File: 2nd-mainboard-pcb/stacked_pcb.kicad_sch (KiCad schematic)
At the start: 7 parts, among them J17 Steckverbinder_Male_1, J18 Steckverbinder_Male_2, J19 Steckverbinder_Female_2

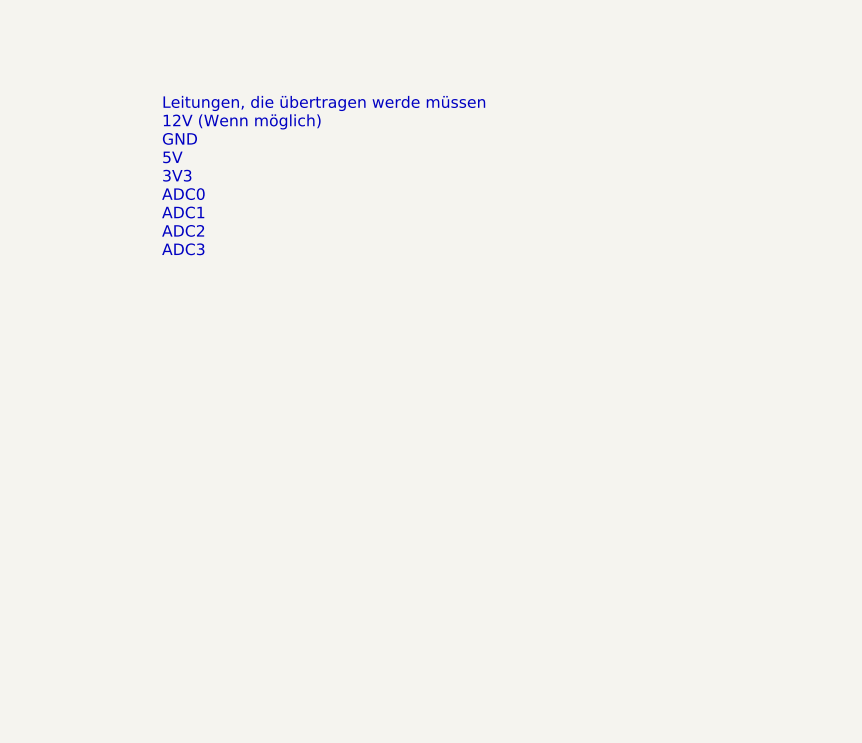
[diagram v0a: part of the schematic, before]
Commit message: added imported components, changed structure
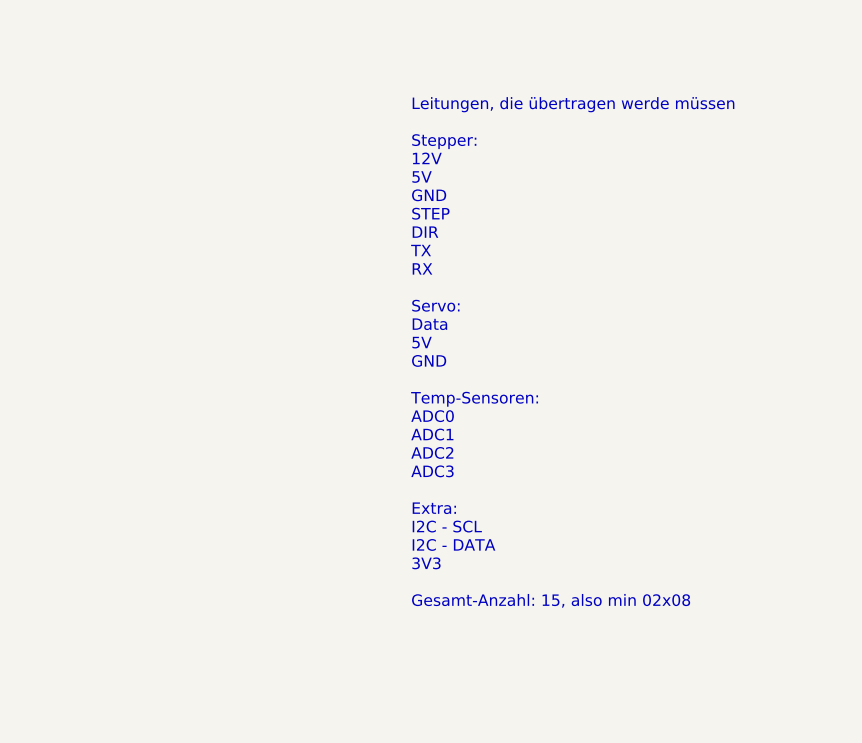
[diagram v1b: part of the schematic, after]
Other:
- note added: "Leitungen, die übertragen werde müssen Stepper: 12V 5V GND STEP DIR TX RX Servo: Data 5V GND Temp-Sensoren: ADC0 ADC1 ADC2 ADC3 Extra: I2C - SCL I2C - DATA 3V3 Gesamt-Anzahl: 15, also min 02x08"
- note removed: "Leitungen, die übertragen werde müssen 12V (Wenn möglich) GND 5V 3V3 ADC0 ADC1 ADC2 ADC3"
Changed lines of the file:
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@@
 		)
 	)
-	(text "Leitungen, die übertragen werde müssen\n12V (Wenn möglich)\nGND\n5V\n3V3\nADC0\nADC1\nADC2\nADC3\n"
+	(text "Leitungen, die übertragen werde müssen\n\nStepper:\n12V\n5V\nGND\nSTEP\nDIR\nTX\nRX\n\nServo:\nData\n5V\nGND\n\nTemp-Sensoren:\nADC0\nADC1\nADC2\nADC3\n\nExtra:\nI2C - SCL\nI2C - DATA\n3V3\n\nGesamt-Anzahl: 15, also min 02x08\n"
 		(exclude_from_sim no)
-		(at 205.74 35.814 0)
+		(at 233.426 55.372 0)
 		(effects
 			(font

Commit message: finished stacked design, annotaded
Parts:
- removed J18: Steckverbinder_Male_2, CustomFotLibByJan:BF100-16-A-D-1-0640-L-C, symbol Connector_Generic:Conn_02x08_Row_Letter_First
- added J21: Steckverbinder_Male_2, CustomFotLibByJan:BF100-16-A-D-1-0640-L-C, symbol Connector_Generic:Conn_02x08_Row_Letter_First
- renumbered J17 to J20, J19 to J22
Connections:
- net +12V: now also J22.b2 (Pin_b2), J21.b2 (Pin_b2); no longer J20.a2 (Pin_a2), J22.a7 (Pin_a7), J22.b7 (Pin_b7)
- net +3V3: now also J22.b4 (Pin_b4), J21.b4 (Pin_b4); no longer J20.a4 (Pin_a4), J22.a5 (Pin_a5), J22.b5 (Pin_b5)
- net GND: now also J21.b1 (Pin_b1); no longer J20.a1 (Pin_a1), J20.a8 (Pin_a8), J20.b8 (Pin_b8), J22.a1 (Pin_a1), J22.a8 (Pin_a8), J22.b8 (Pin_b8)
- net SCL: now also J20.a7 (Pin_a7), J22.a7 (Pin_a7), J21.a7 (Pin_a7); no longer J20.a5 (Pin_a5), J20.b5 (Pin_b5), J22.a4 (Pin_a4), J22.b4 (Pin_b4)
- net SDA: now also J20.a8 (Pin_a8), J22.a8 (Pin_a8), J21.a8 (Pin_a8); no longer J20.a6 (Pin_a6), J20.b6 (Pin_b6), J22.a3 (Pin_a3), J22.b3 (Pin_b3)
- removed net +5V: J20.a3 (Pin_a3), J20.b3 (Pin_b3), J22.a6 (Pin_a6), J22.b6 (Pin_b6)
- removed net IO3: J20.a7 (Pin_a7), J20.b7 (Pin_b7), J22.a2 (Pin_a2), J22.b2 (Pin_b2)
- new net +5V_POW: J20.b3 (Pin_b3), J21.b3 (Pin_b3), J22.b3 (Pin_b3)
- new net ADC0: J20.b5 (Pin_b5), J21.b5 (Pin_b5), J22.b5 (Pin_b5)
- new net ADC1: J20.b6 (Pin_b6), J21.b6 (Pin_b6), J22.b6 (Pin_b6)
- new net ADC2: J20.b7 (Pin_b7), J21.b7 (Pin_b7), J22.b7 (Pin_b7)
- new net ADC3: J20.b8 (Pin_b8), J21.b8 (Pin_b8), J22.b8 (Pin_b8)
- new net DIR: J20.a4 (Pin_a4), J21.a4 (Pin_a4), J22.a4 (Pin_a4)
- new net RESET: J20.a3 (Pin_a3), J21.a3 (Pin_a3), J22.a3 (Pin_a3)
- new net RXD: J20.a6 (Pin_a6), J21.a6 (Pin_a6), J22.a6 (Pin_a6)
- new net SM_Servo: J20.a1 (Pin_a1), J21.a1 (Pin_a1), J22.a1 (Pin_a1)
- new net STEP: J20.a2 (Pin_a2), J21.a2 (Pin_a2), J22.a2 (Pin_a2)
- new net TXD: J20.a5 (Pin_a5), J21.a5 (Pin_a5), J22.a5 (Pin_a5)
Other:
- note added: "Leitungen, die übertragen werde müssen Stepper: 12V 5V GND STEP DIR TX RX RESET Servo: Data 5V GND Temp-Sensoren: ADC0 ADC1 ADC2 ADC3 Extra: I2C - SCL I2C - DATA 3V3 Gesamt-Anzahl: 16, also min 02x08 Optional: BL-Touch Servo Data_BLT 5V GND BL-Touch IO BLT_Switch GND"
- note removed: "Leitungen, die übertragen werde müssen Stepper: 12V 5V GND STEP DIR TX RX Servo: Data 5V GND Temp-Sensoren: ADC0 ADC1 ADC2 ADC3 Extra: I2C - SCL I2C - DATA 3V3 Gesamt-Anzahl: 15, also min 02x08"
- moved on the sheet: J20, J22

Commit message: alle bauteile hinzugefügt
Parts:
- added H1, H10, H11, H12, H2, H3, H4, H9: MountHole, MountingHole:MountingHole_2.2mm_M2_Pad_TopBottom, symbol Mechanical:MountingHole_Pad
- added J19: Steckverbinder_Male_2, CustomFotLibByJan:BF100-16-A-D-1-0640-L-C, symbol Connector_Generic:Conn_02x08_Row_Letter_First
- added J20: Steckverbinder_Female_2, CustomFotLibByJan:BF030-16A-B1-0360-0277-0600-LB, symbol Connector_Generic:Conn_02x08_Row_Letter_First
- renumbered H1 to H5, H2 to H6, H3 to H7, H4 to H8, J20 to J16, J21 to J17, J22 to J18
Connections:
- net +12V: now also J19.b2 (Pin_b2), J20.b2 (Pin_b2)
- net +3V3: now also J19.b4 (Pin_b4), J20.b4 (Pin_b4)
- net +5V_POW: now also J19.b3 (Pin_b3), J20.b3 (Pin_b3)
- net ADC0: now also J19.b5 (Pin_b5), J20.b5 (Pin_b5)
- net ADC1: now also J19.b6 (Pin_b6), J20.b6 (Pin_b6)
- net ADC2: now also J19.b7 (Pin_b7), J20.b7 (Pin_b7)
- net ADC3: now also J19.b8 (Pin_b8), J20.b8 (Pin_b8)
- net DIR: now also J19.a4 (Pin_a4), J20.a4 (Pin_a4)
- net GND: now also H1.1, H10.1, H11.1, H12.1, H2.1, H3.1, H4.1, H9.1, J19.b1 (Pin_b1), J20.b1 (Pin_b1)
- net RESET: now also J19.a3 (Pin_a3), J20.a3 (Pin_a3)
- net RXD: now also J19.a6 (Pin_a6), J20.a6 (Pin_a6)
- net SCL: now also J19.a7 (Pin_a7), J20.a7 (Pin_a7)
- net SDA: now also J19.a8 (Pin_a8), J20.a8 (Pin_a8)
- net SM_Servo: now also J19.a1 (Pin_a1), J20.a1 (Pin_a1)
- net STEP: now also J19.a2 (Pin_a2), J20.a2 (Pin_a2)
- net TXD: now also J19.a5 (Pin_a5), J20.a5 (Pin_a5)
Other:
- note added: "Leitungen, die übertragen werde müssen Fans: 12V 5V GND PWM0 PWM1 PWM2 PWM3 Extra: I2C - SCL I2C - DATA 3V3 Gesamt-Anzahl: 16, also min 02x08"
- note added: "Modul 1: Fans"
- note added: "Modul 2: Atmega + Leistungs-Eingänge"
- note added: "Modul 3: Motoren"
- note removed: "Modul 1"
- note removed: "Modul 2"

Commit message: module 1 positioniert
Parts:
- J16: value Steckverbinder_Male_1 -> Steckverbinder_Male_Fans
- J17: value Steckverbinder_Male_2 -> Steckverbinder_Male_Leistung
- J18: value Steckverbinder_Female_2 -> Steckverbinder_Female_Leistung
- J19: value Steckverbinder_Male_2 -> Steckverbinder_Male_Motoren
- J20: value Steckverbinder_Female_2 -> Steckverbinder_Female_Motoren
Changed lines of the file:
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@@
 			)
 		)
-		(property "Value" "Steckverbinder_Male_2"
+		(property "Value" "Steckverbinder_Male_Leistung"
 			(at 120.65 26.67 0)
 			(effects
@@
 			)
 		)
-		(property "Value" "Steckverbinder_Male_1"
+		(property "Value" "Steckverbinder_Male_Fans"
 			(at 46.99 26.67 0)
 			(effects
@@
 			)
 		)
-		(property "Value" "Steckverbinder_Female_2"
+		(property "Value" "Steckverbinder_Female_Motoren"
 			(at 95.25 114.3 0)
 			(effects
@@
 			)
 		)
-		(property "Value" "Steckverbinder_Male_2"
+		(property "Value" "Steckverbinder_Male_Motoren"
 			(at 45.72 114.3 0)
 			(effects
@@
 			)
 		)
-		(property "Value" "Steckverbinder_Female_2"
+		(property "Value" "Steckverbinder_Female_Leistung"
 			(at 170.18 26.67 0)
 			(effects

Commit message: new arrangement pcb
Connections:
- net +12V: now also J18.a2 (Pin_a2); no longer J18.b2 (Pin_b2)
- net +3V3: now also J18.a4 (Pin_a4); no longer J18.b4 (Pin_b4)
- net +5V_POW: now also J18.a3 (Pin_a3); no longer J18.b3 (Pin_b3)
- net ADC0: now also J16.a2 (Pin_a2), J18.b2 (Pin_b2); no longer J16.b5 (Pin_b5), J17.b5 (Pin_b5), J18.b5 (Pin_b5)
- net ADC1: now also J16.a3 (Pin_a3), J18.b3 (Pin_b3); no longer J16.b6 (Pin_b6), J17.b6 (Pin_b6), J18.b6 (Pin_b6)
- net ADC2: now also J16.a6 (Pin_a6), J18.b6 (Pin_b6); no longer J16.b7 (Pin_b7), J17.b7 (Pin_b7), J18.b7 (Pin_b7)
- net ADC3: now also J16.a7 (Pin_a7), J18.b7 (Pin_b7); no longer J16.b8 (Pin_b8), J17.b8 (Pin_b8), J18.b8 (Pin_b8)
- net DIR: no longer J16.a4 (Pin_a4), J18.a4 (Pin_a4)
- net GND: now also J18.a1 (Pin_a1); no longer J18.b1 (Pin_b1)
- net RESET: now also J16.b5 (Pin_b5), J18.a5 (Pin_a5); no longer J16.a3 (Pin_a3), J18.a3 (Pin_a3)
- net RXD: no longer J16.a6 (Pin_a6), J18.a6 (Pin_a6)
- net SCL: now also J16.b8 (Pin_b8), J18.a8 (Pin_a8); no longer J16.a7 (Pin_a7), J18.a7 (Pin_a7)
- net SDA: now also J16.b7 (Pin_b7), J18.a7 (Pin_a7); no longer J16.a8 (Pin_a8), J18.a8 (Pin_a8)
- net SM_Servo: no longer J16.a1 (Pin_a1), J18.a1 (Pin_a1)
- net STEP: no longer J16.a2 (Pin_a2), J18.a2 (Pin_a2)
- net TXD: no longer J16.a5 (Pin_a5), J18.a5 (Pin_a5)
- new net BLT_Servo: J17.b5 (Pin_b5)
- new net BLT_Switch: J17.b6 (Pin_b6)
- new net FAN_01_PWM_clockwise: J16.a5 (Pin_a5), J18.b5 (Pin_b5)
- new net FAN_01_PWM_counterclockwise: J16.a4 (Pin_a4), J18.b4 (Pin_b4)
- new net FAN_2_PWM: J16.a1 (Pin_a1), J18.b1 (Pin_b1)
- new net FAN_3_PWM: J16.a8 (Pin_a8), J18.b8 (Pin_b8)
- new net LED_2: J16.b6 (Pin_b6), J18.a6 (Pin_a6)
- new net LED_3: J17.b7 (Pin_b7)
- new net SMD_TEMP_1: J17.b8 (Pin_b8)
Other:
- moved on the sheet: J16, J17, J18

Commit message: fertgie V1 der Leistungs-Platine
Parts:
- added J24: Steckverbinder_Male_Fans, Imported_Component_Footprints:SAMTEC_TSM-107-04-L-DV, symbol Imported_Component_Symbols:TSM-107-04-L-DV
- added J25: HLE-107-02-L-DV, Imported_Component_Footprints:SAMTEC_HLE-107-02-L-DV, symbol Imported_Component_Symbols:HLE-107-02-L-DV
- added J26: Steckverbinder_Male_Leistung, Imported_Component_Footprints:SAMTEC_TSM-107-04-L-DV, symbol Imported_Component_Symbols:TSM-107-04-L-DV
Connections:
- net ADC0: now also J18.b7 (Pin_b7); no longer J18.b2 (Pin_b2)
- net ADC1: now also J18.b6 (Pin_b6); no longer J18.b3 (Pin_b3)
- net ADC2: now also J18.b3 (Pin_b3); no longer J18.b6 (Pin_b6)
- net ADC3: now also J18.b2 (Pin_b2); no longer J18.b7 (Pin_b7)
- net BLT_Servo: now also J17.a3 (Pin_a3); no longer J17.b5 (Pin_b5)
- net LED_3: now also J17.a8 (Pin_a8); no longer J17.b7 (Pin_b7)
- net RESET: now also J17.b5 (Pin_b5); no longer J17.a3 (Pin_a3)
- net SCL: now also J17.b8 (Pin_b8); no longer J17.a7 (Pin_a7)
- net SDA: now also J17.b7 (Pin_b7); no longer J17.a8 (Pin_a8)
- net SMD_TEMP_1: now also J17.a7 (Pin_a7); no longer J17.b8 (Pin_b8)

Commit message: Fan-PCB-Beginning
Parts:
- removed J16: Steckverbinder_Male_Fans, CustomFotLibByJan:BF100-16-A-D-1-0640-L-C, symbol Connector_Generic:Conn_02x08_Row_Letter_First
- removed J17: Steckverbinder_Male_Leistung, CustomFotLibByJan:BF100-16-A-D-1-0640-L-C, symbol Connector_Generic:Conn_02x08_Row_Letter_First
- removed J18: Steckverbinder_Female_Leistung, CustomFotLibByJan:BF030-16A-B1-0360-0277-0600-LB, symbol Connector_Generic:Conn_02x08_Row_Letter_First
- removed J19: Steckverbinder_Male_Motoren, CustomFotLibByJan:BF100-16-A-D-1-0640-L-C, symbol Connector_Generic:Conn_02x08_Row_Letter_First
- removed J20: Steckverbinder_Female_Motoren, CustomFotLibByJan:BF030-16A-B1-0360-0277-0600-LB, symbol Connector_Generic:Conn_02x08_Row_Letter_First
- added J15: Steckverbinder_Female_Motoren, Imported_Component_Footprints:SAMTEC_HLE-107-02-L-DV, symbol Imported_Component_Symbols:HLE-107-02-L-DV
- J13: renamed from J25; value HLE-107-02-L-DV -> Steckverbinder_Female_Leistung
- renumbered J24 to J12, J26 to J14
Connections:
- net +12V: now also J12.03, J13.03, J14.03, J15.03
- net +5V_POW: now also J12.05, J13.05, J14.05, J15.05
- net ADC0: now also J12.08, J13.06, J15.08
- net ADC1: now also J12.10, J13.08, J15.10
- net ADC2: now also J12.12, J13.10, J15.12
- net ADC3: now also J12.14, J13.12, J15.14
- net BLT_Servo: now also J14.10
- net BLT_Switch: now also J14.12
- net DIR: now also J14.08
- net FAN_01_PWM_clockwise: now also J12.04, J13.07, J15.04
- net FAN_01_PWM_counterclockwise: now also J12.02, J13.09, J15.02
- net FAN_2_PWM: now also J12.13, J13.13, J15.06
- net FAN_3_PWM: now also J12.11, J13.11, J15.11
- net GND: now also J12.01, J13.01, J14.01, J15.01
- net LED_2: now also J12.09, J13.04
- net LED_3: now also J14.11, J15.07
- net RESET: now also J15.09
- net RXD: now also J14.04
- net SCL: now also J14.14
- net SDA: now also J14.02
- net SM_Servo: now also J14.09
- net STEP: now also J14.07
- net TXD: now also J14.06
- net SMD_TEMP_0: now reaches J12.06
- net SMD_TEMP_0: now also J13.14, J15.13
- net +5V_USBC: now reaches J12.07
- net +5V_USBC: now also J13.02
- no-connect marks 0 -> 1
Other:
- moved on the sheet: J12, J13, J14

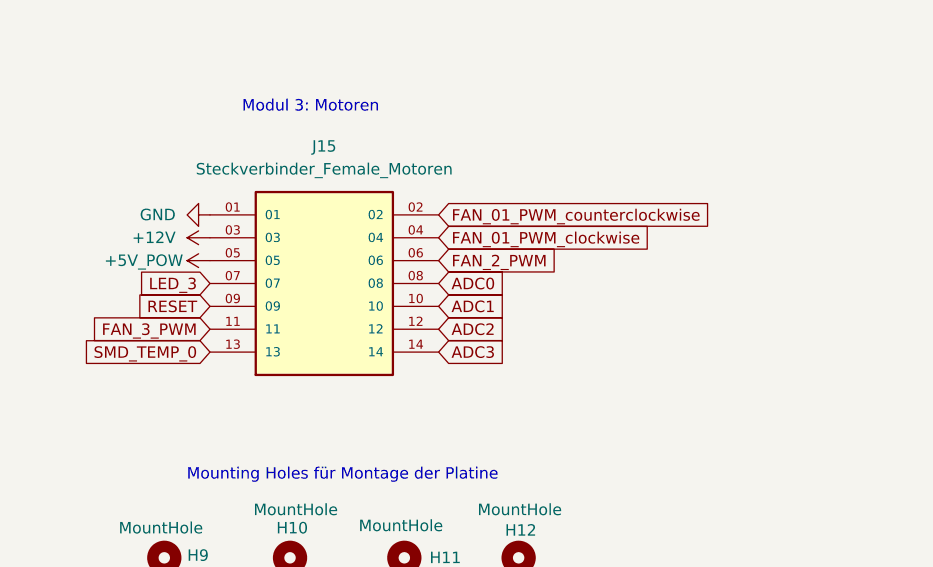
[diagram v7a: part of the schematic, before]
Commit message: pcb fans finished, pcb motors begin
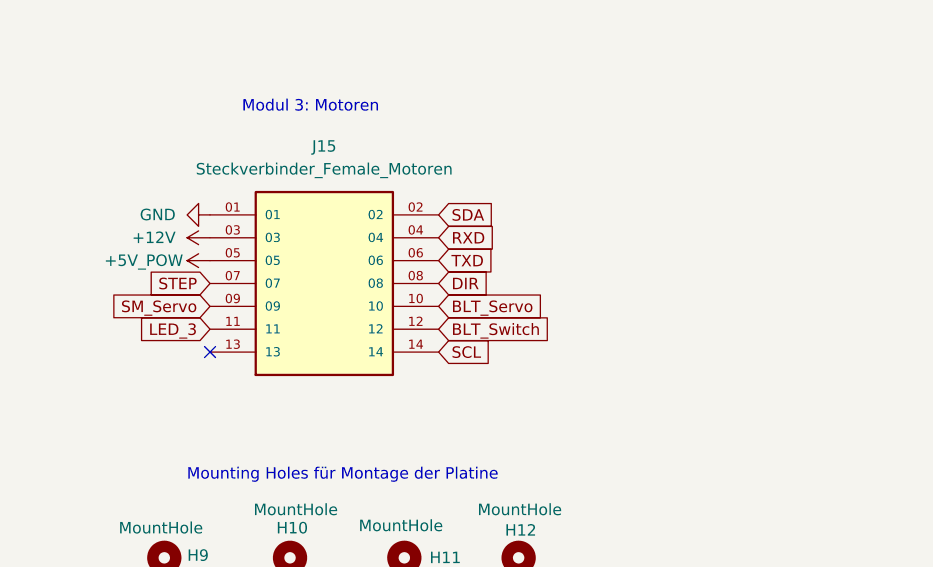
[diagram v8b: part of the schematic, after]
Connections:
- net RESET is gone; now on net SM_Servo: J15.09
- net ADC0: no longer J15.08
- net ADC1: no longer J15.10
- net ADC2: no longer J15.12
- net ADC3: no longer J15.14
- net BLT_Servo: now also J15.10
- net BLT_Switch: now also J15.12
- net DIR: now also J15.08
- net FAN_01_PWM_clockwise: no longer J15.04
- net FAN_01_PWM_counterclockwise: no longer J15.02
- net FAN_2_PWM: no longer J15.06
- net FAN_3_PWM: no longer J15.11
- net LED_3: now also J15.11; no longer J15.07
- net RXD: now also J15.04
- net SCL: now also J15.14
- net SDA: now also J15.02
- net SMD_TEMP_0: no longer J15.13
- net STEP: now also J15.07
- net TXD: now also J15.06
- no-connect marks 1 -> 2
